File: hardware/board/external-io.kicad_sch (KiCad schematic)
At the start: 14 parts, among them J1401 Ext Audio, J1401 Ext FG, J1401 Ext Inst AD, J1401 Ext Inst BC, J1401 Ext MM, J1401 Ext Osc AD, J1401 Ext Osc BC

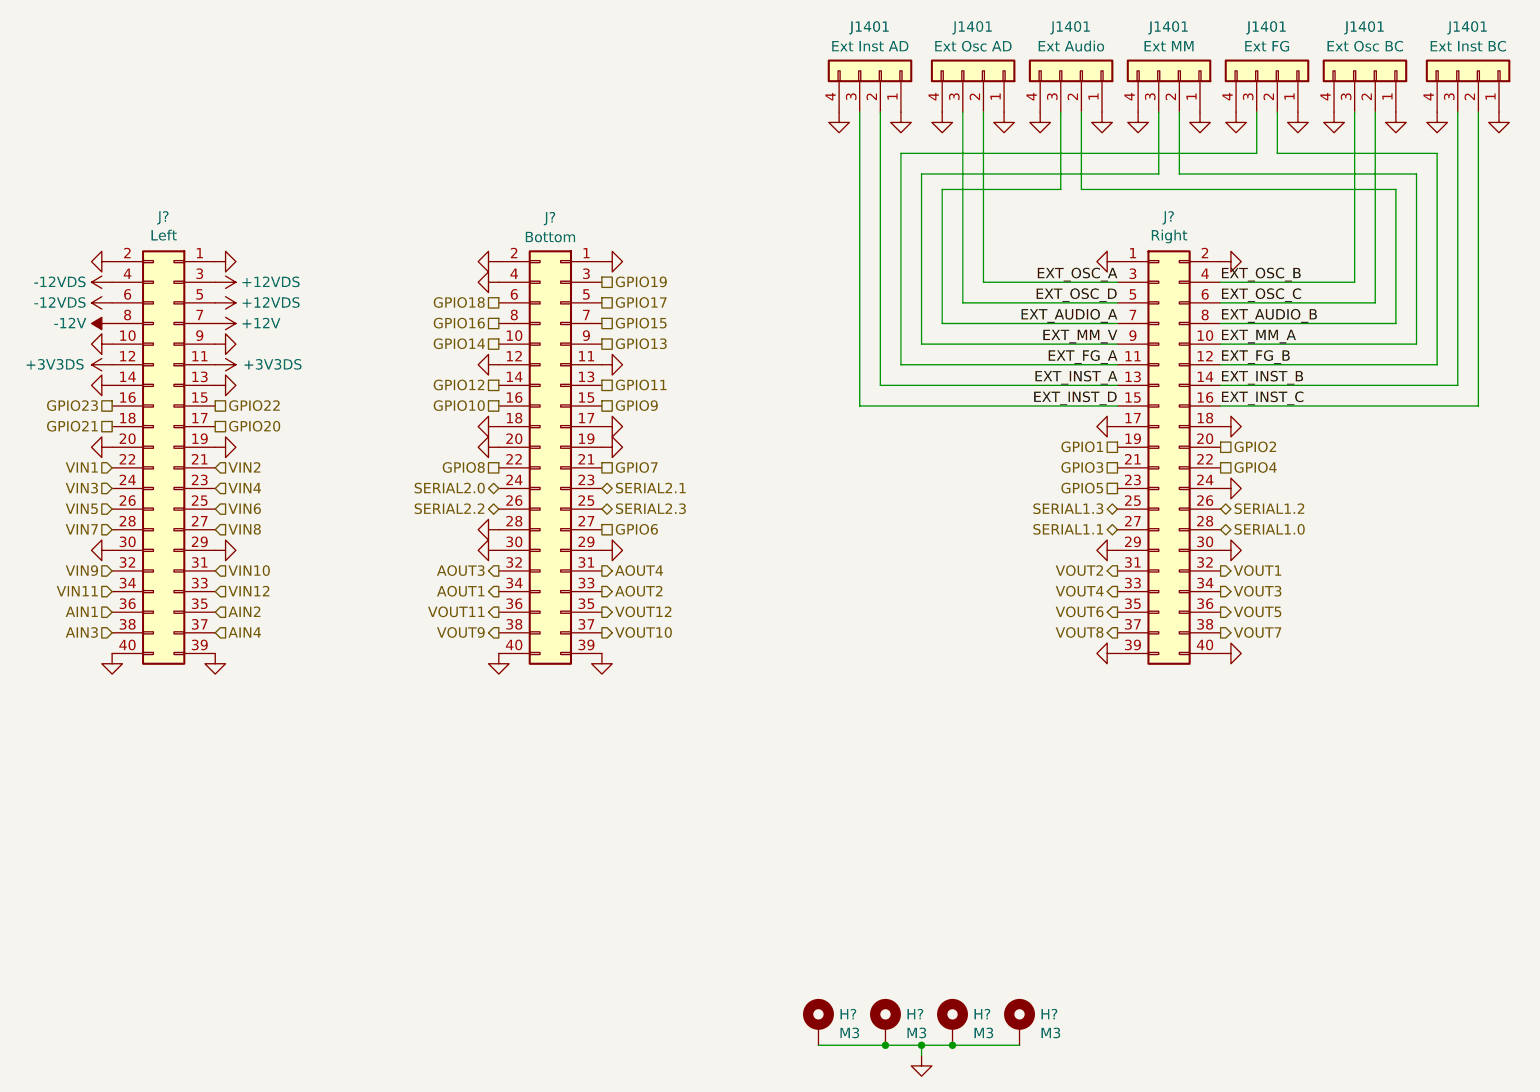
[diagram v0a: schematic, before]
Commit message: Update resistor values in Vout DAC buffers
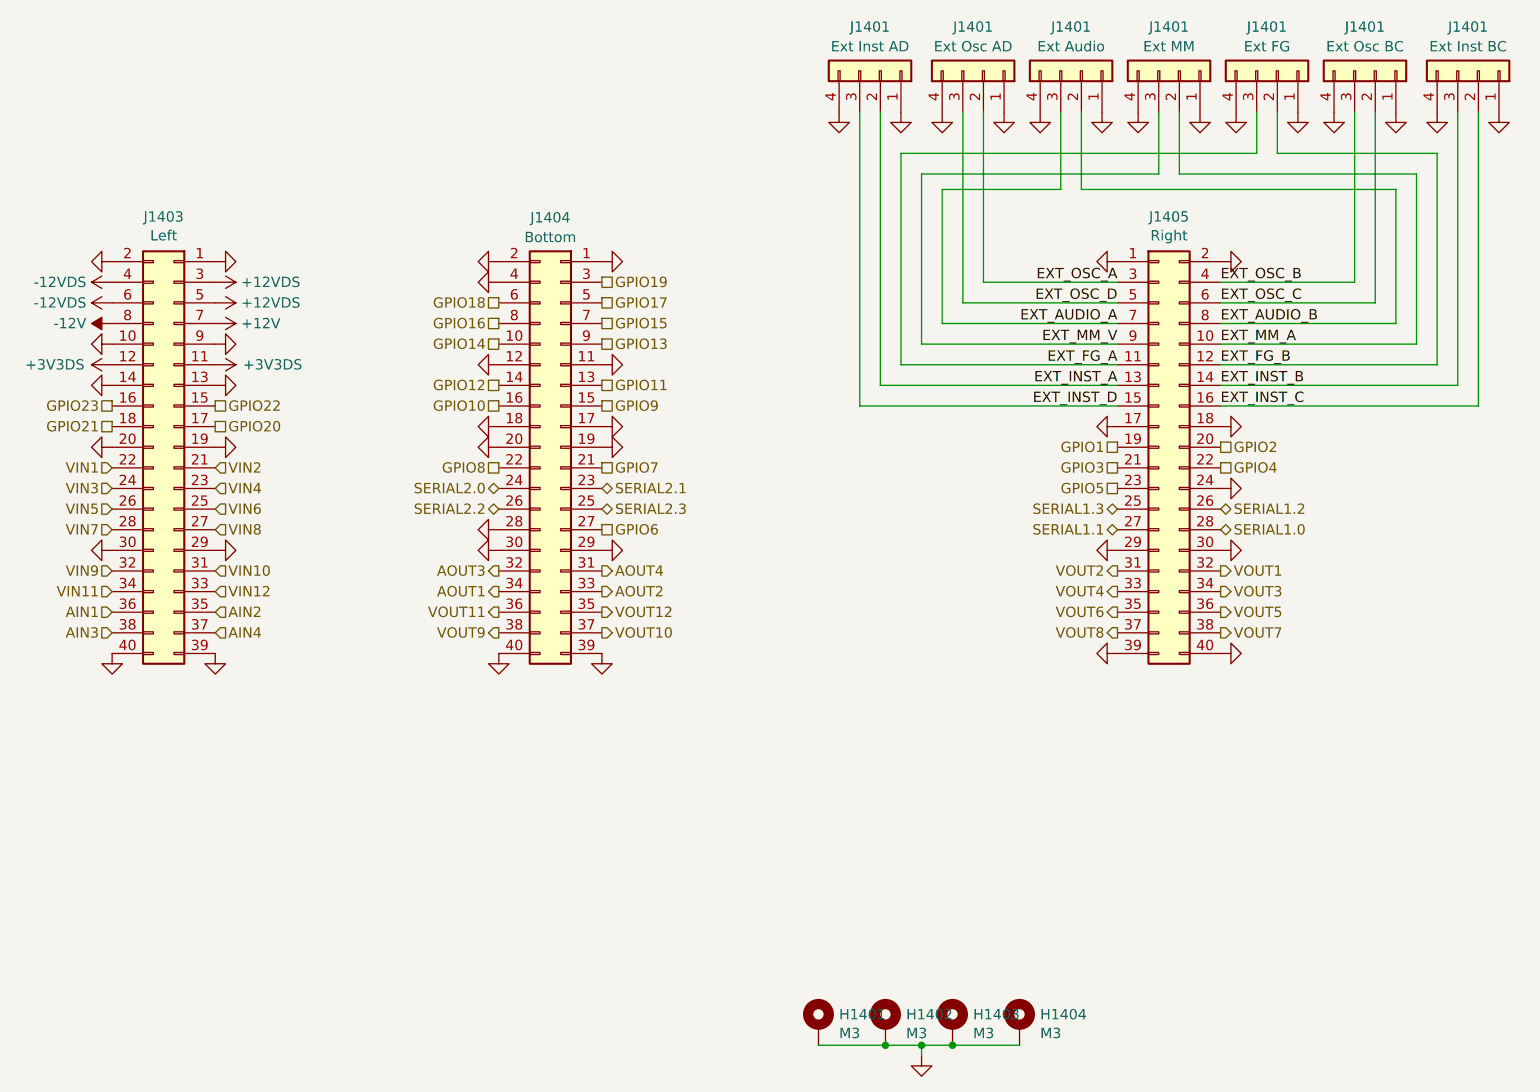
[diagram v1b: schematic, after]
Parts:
- gave numbers to parts that had none: 7
